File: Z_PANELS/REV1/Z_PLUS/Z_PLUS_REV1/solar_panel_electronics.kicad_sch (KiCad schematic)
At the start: 34 parts, among them U3 LTC3130EUDC-1-PBF

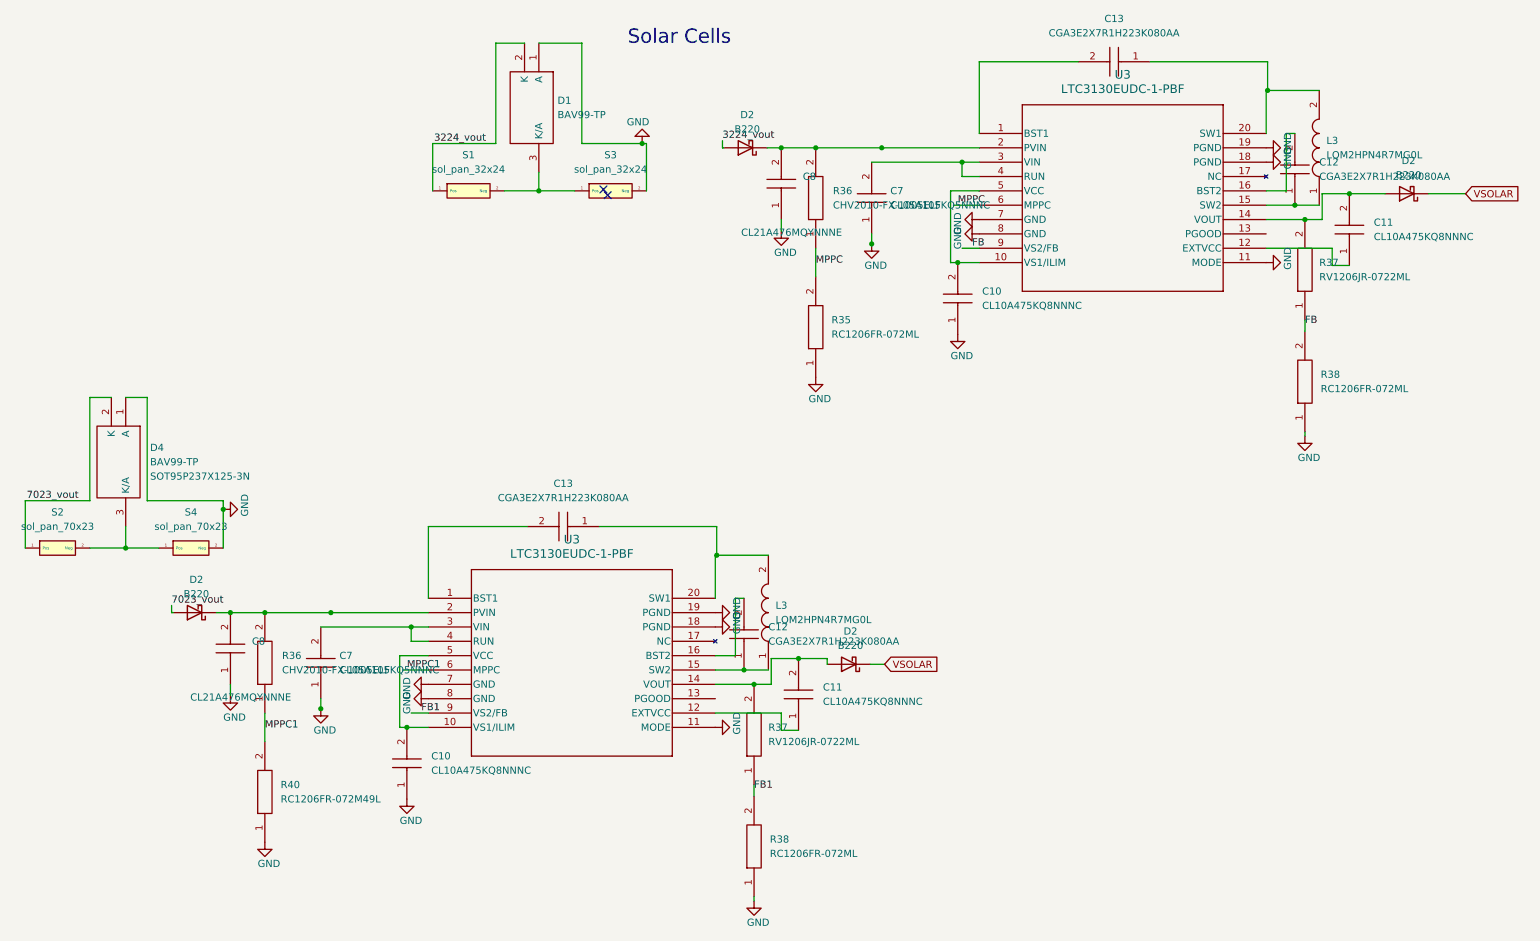
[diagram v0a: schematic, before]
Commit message: added dxf to z plus. incremental update
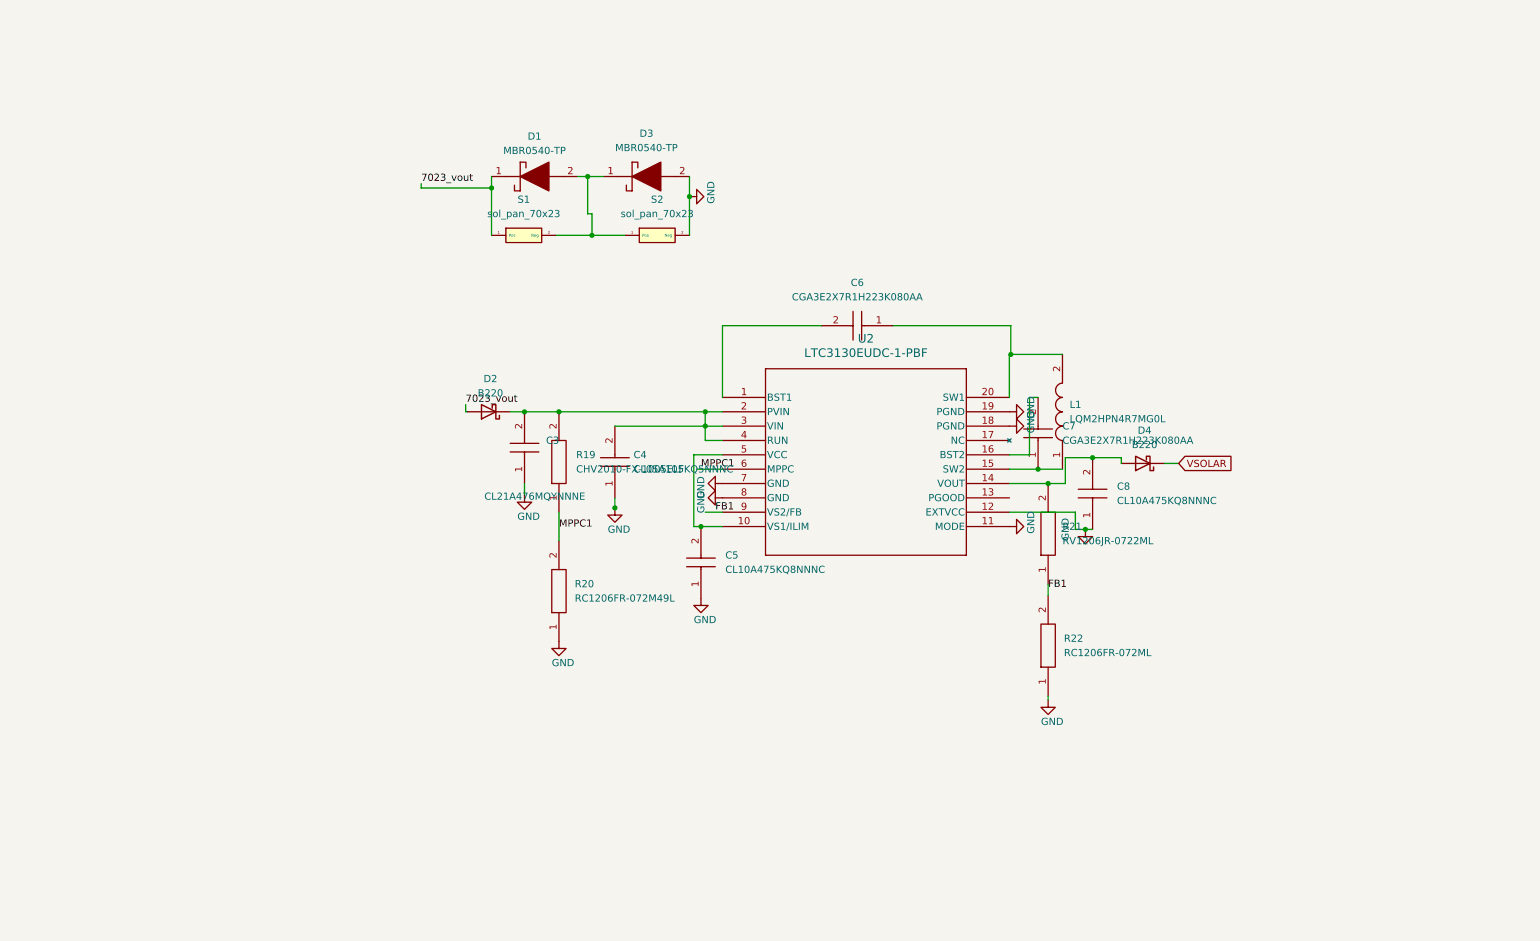
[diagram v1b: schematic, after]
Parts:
- removed C10 (x2), C11 (x2): CL10A475KQ8NNNC, CAPC1608X90N, symbol AA_AUTO_LOADER:CL10A475KQ8NNNC
- removed C12 (x2), C13 (x2): CGA3E2X7R1H223K080AA, CAPC1608X90N, symbol AA_AUTO_LOADER:CGA3E2X7R1H223K080AA
- removed C7 (x2): CL05A105KQ5NNNC, CAPC1005X55N, symbol AA_AUTO_LOADER:CL05A105KQ5NNNC
- removed C8 (x2): CL21A476MQYNNNE, CAPC2012X135N, symbol AA_AUTO_LOADER:CL21A476MQYNNNE
- removed D1, D4: BAV99-TP, SOT95P237X125-3N, symbol AA_AUTO_LOADER:BAV99-TP
- removed D2 (x4): B220, Diode_SMD:D_SMB, symbol Diode:B220
- removed L3 (x2): LQM2HPN4R7MG0L, LQM2HPN1R0MG0L, symbol AA_AUTO_LOADER:LQM2HPN4R7MG0L
- removed R35, R38 (x2): RC1206FR-072ML, RESC3116X65N, symbol AA_AUTO_LOADER:RC1206FR-072ML
- removed R36 (x2): CHV2010-FX-1005ELF, RESC5025X70N, symbol AA_AUTO_LOADER:CHV2010-FX-1005ELF
- removed R37 (x2): RV1206JR-0722ML, RESC3116X65N, symbol AA_AUTO_LOADER:RV1206JR-0722ML
- removed R40: RC1206FR-072M49L, RESC3116X65N, symbol AA_AUTO_LOADER:RC1206FR-072M49L
- removed S1, S3: sol_pan_32x24, CUSTOM_SOLAR_2432:solar_panel_SM500K12TF_32x24, symbol solar_symbol_lib:sol_pan_32x24
- removed S4: sol_pan_70x23, CUSTOM_SOLAR_7023:sol_pan_SM141K10TFS_70x23, symbol solar_symbol_lib:sol_pan_70x23
- removed U3 (x2): LTC3130EUDC-1-PBF, UDC_20_ADI, symbol LTC3130:LTC3130EUDC-1-PBF
- added C3: CL21A476MQYNNNE, CAPC2012X135N, symbol AA_AUTO_LOADER:CL21A476MQYNNNE
- added C4: CL05A105KQ5NNNC, CAPC1005X55N, symbol AA_AUTO_LOADER:CL05A105KQ5NNNC
- added C5, C8: CL10A475KQ8NNNC, CAPC1608X90N, symbol AA_AUTO_LOADER:CL10A475KQ8NNNC
- added C6, C7: CGA3E2X7R1H223K080AA, CAPC1608X90N, symbol AA_AUTO_LOADER:CGA3E2X7R1H223K080AA
- added D1, D3: MBR0540-TP, SOD3716X135N, symbol AA_AUTO_LOADER:MBR0540-TP
- added D2, D4: B220, Diode_SMD:D_SMB, symbol Diode:B220
- added L1: LQM2HPN4R7MG0L, LQM2HPN1R0MG0L, symbol AA_AUTO_LOADER:LQM2HPN4R7MG0L
- added R19: CHV2010-FX-1005ELF, RESC5025X70N, symbol AA_AUTO_LOADER:CHV2010-FX-1005ELF
- added R20: RC1206FR-072M49L, RESC3116X65N, symbol AA_AUTO_LOADER:RC1206FR-072M49L
- added R21: RV1206JR-0722ML, RESC3116X65N, symbol AA_AUTO_LOADER:RV1206JR-0722ML
- added R22: RC1206FR-072ML, RESC3116X65N, symbol AA_AUTO_LOADER:RC1206FR-072ML
- added S1: sol_pan_70x23, CUSTOM_SOLAR_7023:sol_pan_SM141K10TFS_70x23, symbol solar_symbol_lib:sol_pan_70x23
- added U2: LTC3130EUDC-1-PBF, UDC_20_ADI, symbol LTC3130:LTC3130EUDC-1-PBF
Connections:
- net 7023_vout: now also D1.1, D2.2 (A), S1.1 (Pos); no longer S2.1 (Pos)
- net FB1: now also R21.1, R22.2, U2.9 (VS2/FB)
- net GND: now also S2.2 (Neg), C3.1, C4.1, C5.1, C8.1, D3.2, R20.1, R22.1, U2.11 (MODE), U2.12 (EXTVCC), U2.18 (PGND), U2.19 (PGND), U2.7 (GND), U2.8 (GND)
- net MPPC1: now also R19.1, R20.2, U2.6 (MPPC)
- net VSOLAR: now also D4.1 (K)
- new net: C7.1, L1.1, U2.15 (SW2)
- new net: C6.1, L1.2, U2.20 (SW1)
- new net: C5.2, U2.10 (VS1/ILIM), U2.5 (VCC)
- new net: C8.2, D4.2 (A), R21.2, U2.14 (VOUT)
- new net: C3.2, C4.2, D2.1 (K), R19.2, U2.2 (PVIN), U2.3 (VIN), U2.4 (RUN)
- new net: D1.2, D3.1, S1.2 (Neg), S2.1 (Pos)
- new net: C6.2, U2.1 (BST1)
- new net: C7.2, U2.16 (BST2)
- no-connect marks 2 -> 0
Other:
- note removed: "Solar Cells"

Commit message: made changes to Z plus board
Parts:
- removed D1, D3: MBR0540-TP, SOD3716X135N, symbol AA_AUTO_LOADER:MBR0540-TP
- removed D2, D4: B220, Diode_SMD:D_SMB, symbol Diode:B220
- removed S1, S2: sol_pan_70x23, CUSTOM_SOLAR_7023:sol_pan_SM141K10TFS_70x23, symbol solar_symbol_lib:sol_pan_70x23
- added D1, D2, D3, D5, D6, D7: RB521S30T1G, SODFL1608X70N, symbol AA_AUTO_LOADER:RB521S30T1G
- added IC2, IC3, IC4, IC5: SM141K04TFV, SODFL490150X120N, symbol AA_AUTO_LOADER:SM141K04TFV
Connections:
- net 7023_vout: now also D3.1, D7.2, IC2.1 (POS)
- net GND: now also D6.2, IC5.2 (NEG)
- net VSOLAR: now also D2.1
- net at C8.2, R21.2, U2.14 (VOUT): now also D2.2
- net at C3.2, C4.2, R19.2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: now also D7.1
- new net: D1.1, D3.2, IC2.2 (NEG), IC3.1 (POS)
- new net: D1.2, D5.1, IC3.2 (NEG), IC4.1 (POS)
- new net: D5.2, D6.1, IC4.2 (NEG), IC5.1 (POS)
